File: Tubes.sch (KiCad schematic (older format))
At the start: 36 parts

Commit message: Finished draft schema
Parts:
- gave numbers to parts that had none: 36

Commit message: Finished schema and started PCB layout
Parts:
- R1, R10, R11, R12, R13, R14, R15, R16, R17, R18, R2, R3, R4, R5, R6, R7, R8, R9: footprint (none) -> Resistor_THT:R_Axial_DIN0207_L6.3mm_D2.5mm_P10.16mm_Horizontal
- U10, U2, U3, U4, U8, U9: footprint (none) -> nixies:Nixie_ZM1000
- U11, U12, U13, U5, U6, U7: footprint (none) -> Package_DIP:DIP-16_W7.62mm_LongPads
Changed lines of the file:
@@
 F 0 "U10" H 9828 5003 60  0000 L CNN
 F 1 "ZM1000" H 9828 4897 60  0000 L CNN
-F 2 "" V 8950 4600 60  0001 C CNN
+F 2 "nixies:Nixie_ZM1000" V 8950 4600 60  0001 C CNN
 F 3 "" V 8950 4600 60  0001 C CNN
 	1    8800 4650
@@
 F 0 "U9" H 6228 5003 60  0000 L CNN
 F 1 "ZM1000" H 6228 4897 60  0000 L CNN
-F 2 "" V 5350 4600 60  0001 C CNN
+F 2 "nixies:Nixie_ZM1000" V 5350 4600 60  0001 C CNN
 F 3 "" V 5350 4600 60  0001 C CNN
 	1    5200 4650
@@
 F 0 "U8" H 2628 5003 60  0000 L CNN
 F 1 "ZM1000" H 2628 4897 60  0000 L CNN
-F 2 "" V 1750 4600 60  0001 C CNN
+F 2 "nixies:Nixie_ZM1000" V 1750 4600 60  0001 C CNN
 F 3 "" V 1750 4600 60  0001 C CNN
 	1    1600 4650
@@
 F 0 "U2" H 2628 2303 60  0000 L CNN
 F 1 "ZM1000" H 2628 2197 60  0000 L CNN
-F 2 "" V 1750 1900 60  0001 C CNN
+F 2 "nixies:Nixie_ZM1000" V 1750 1900 60  0001 C CNN
 F 3 "" V 1750 1900 60  0001 C CNN
 	1    1600 1950
@@
 F 0 "U3" H 6228 2303 60  0000 L CNN
 F 1 "ZM1000" H 6228 2197 60  0000 L CNN
-F 2 "" V 5350 1900 60  0001 C CNN
+F 2 "nixies:Nixie_ZM1000" V 5350 1900 60  0001 C CNN
 F 3 "" V 5350 1900 60  0001 C CNN
 	1    5200 1950
@@
 F 0 "U4" H 9828 2303 60  0000 L CNN
 F 1 "ZM1000" H 9828 2197 60  0000 L CNN
-F 2 "" V 8950 1900 60  0001 C CNN
+F 2 "nixies:Nixie_ZM1000" V 8950 1900 60  0001 C CNN
 F 3 "" V 8950 1900 60  0001 C CNN
 	1    8800 1950
@@
 F 0 "U13" V 9800 5200 50  0000 R CNN
 F 1 "SN74141" V 9800 4850 50  0000 R CNN
-F 2 "" H 9900 4900 50  0001 C CNN
+F 2 "Package_DIP:DIP-16_W7.62mm_LongPads" H 9900 4900 50  0001 C CNN
 F 3 "http://www.ti.com/lit/ds/symlink/sn74hc595.pdf" H 9900 4900 50  0001 C CNN
 	1    9900 4850
@@
 F 0 "R16" V 9407 3900 50  0000 C CNN
 F 1 "10M" V 9316 3900 50  0000 C CNN
-F 2 "" V 9130 3900 50  0001 C CNN
+F 2 "Resistor_THT:R_Axial_DIN0207_L6.3mm_D2.5mm_P10.16mm_Horizontal" V 9130 3900 50  0001 C CNN
 F 3 "~" H 9200 3900 50  0001 C CNN
 	1    9200 3900
@@
 F 0 "U12" V 6200 5200 50  0000 R CNN
 F 1 "SN74141" V 6200 4850 50  0000 R CNN
-F 2 "" H 6300 4900 50  0001 C CNN
+F 2 "Package_DIP:DIP-16_W7.62mm_LongPads" H 6300 4900 50  0001 C CNN
 F 3 "http://www.ti.com/lit/ds/symlink/sn74hc595.pdf" H 6300 4900 50  0001 C CNN
 	1    6300 4850
@@
 $EndComp
 Wire Wire Line
-	6300 4200 6300 4100
-Wire Wire Line
 	6300 4100 6400 4100
 Text HLabel 6800 5000 2    50   Input ~ 0
@@
 F 0 "R13" V 5807 3900 50  0000 C CNN
 F 1 "10M" V 5716 3900 50  0000 C CNN
-F 2 "" V 5530 3900 50  0001 C CNN
+F 2 "Resistor_THT:R_Axial_DIN0207_L6.3mm_D2.5mm_P10.16mm_Horizontal" V 5530 3900 50  0001 C CNN
 F 3 "~" H 5600 3900 50  0001 C CNN
 	1    5600 3900
@@
 F 0 "U11" V 2600 5200 50  0000 R CNN
 F 1 "SN74141" V 2600 4850 50  0000 R CNN
-F 2 "" H 2700 4900 50  0001 C CNN
+F 2 "Package_DIP:DIP-16_W7.62mm_LongPads" H 2700 4900 50  0001 C CNN
 F 3 "http://www.ti.com/lit/ds/symlink/sn74hc595.pdf" H 2700 4900 50  0001 C CNN
 	1    2700 4850
@@
 F 0 "R10" V 2207 3900 50  0000 C CNN
 F 1 "10M" V 2116 3900 50  0000 C CNN
-F 2 "" V 1930 3900 50  0001 C CNN
+F 2 "Resistor_THT:R_Axial_DIN0207_L6.3mm_D2.5mm_P10.16mm_Horizontal" V 1930 3900 50  0001 C CNN
 F 3 "~" H 2000 3900 50  0001 C CNN
 	1    2000 3900
@@
 F 0 "U5" V 2600 2500 50  0000 R CNN
 F 1 "SN74141" V 2600 2150 50  0000 R CNN
-F 2 "" H 2700 2200 50  0001 C CNN
+F 2 "Package_DIP:DIP-16_W7.62mm_LongPads" H 2700 2200 50  0001 C CNN
 F 3 "http://www.ti.com/lit/ds/symlink/sn74hc595.pdf" H 2700 2200 50  0001 C CNN
 	1    2700 2150
@@
 F 0 "R1" V 2207 1200 50  0000 C CNN
 F 1 "10M" V 2116 1200 50  0000 C CNN
-F 2 "" V 1930 1200 50  0001 C CNN
+F 2 "Resistor_THT:R_Axial_DIN0207_L6.3mm_D2.5mm_P10.16mm_Horizontal" V 1930 1200 50  0001 C CNN
 F 3 "~" H 2000 1200 50  0001 C CNN
 	1    2000 1200
@@
 F 0 "U6" V 6200 2500 50  0000 R CNN
 F 1 "SN74141" V 6200 2150 50  0000 R CNN
-F 2 "" H 6300 2200 50  0001 C CNN
+F 2 "Package_DIP:DIP-16_W7.62mm_LongPads" H 6300 2200 50  0001 C CNN
 F 3 "http://www.ti.com/lit/ds/symlink/sn74hc595.pdf" H 6300 2200 50  0001 C CNN
 	1    6300 2150
@@
 	0    -1   -1   0
 $EndComp
-Wire Wire Line
-	6300 1500 6300 1400
-Wire Wire Line
-	6300 1400 6400 1400
 Text HLabel 6800 2300 2    50   Input ~ 0
 BCD_T2A
@@
 F 0 "R4" V 5807 1200 50  0000 C CNN
 F 1 "10M" V 5716 1200 50  0000 C CNN
-F 2 "" V 5530 1200 50  0001 C CNN
+F 2 "Resistor_THT:R_Axial_DIN0207_L6.3mm_D2.5mm_P10.16mm_Horizontal" V 5530 1200 50  0001 C CNN
 F 3 "~" H 5600 1200 50  0001 C CNN
 	1    5600 1200
@@
 F 0 "U7" V 9800 2500 50  0000 R CNN
 F 1 "SN74141" V 9800 2150 50  0000 R CNN
-F 2 "" H 9900 2200 50  0001 C CNN
+F 2 "Package_DIP:DIP-16_W7.62mm_LongPads" H 9900 2200 50  0001 C CNN
 F 3 "http://www.ti.com/lit/ds/symlink/sn74hc595.pdf" H 9900 2200 50  0001 C CNN
 	1    9900 2150
@@
 F 0 "R7" V 9407 1200 50  0000 C CNN
 F 1 "10M" V 9316 1200 50  0000 C CNN
-F 2 "" V 9130 1200 50  0001 C CNN
+F 2 "Resistor_THT:R_Axial_DIN0207_L6.3mm_D2.5mm_P10.16mm_Horizontal" V 9130 1200 50  0001 C CNN
 F 3 "~" H 9200 1200 50  0001 C CNN
 	1    9200 1200
@@
 F 0 "R3" V 3457 1200 50  0000 C CNN
 F 1 "10k" V 3366 1200 50  0000 C CNN
-F 2 "" V 3180 1200 50  0001 C CNN
+F 2 "Resistor_THT:R_Axial_DIN0207_L6.3mm_D2.5mm_P10.16mm_Horizontal" V 3180 1200 50  0001 C CNN
 F 3 "~" H 3250 1200 50  0001 C CNN
 	1    3250 1200
@@
 F 0 "R2" H 2270 1246 50  0000 L CNN
 F 1 "100k" H 2270 1155 50  0000 L CNN
-F 2 "" V 2130 1200 50  0001 C CNN
+F 2 "Resistor_THT:R_Axial_DIN0207_L6.3mm_D2.5mm_P10.16mm_Horizontal" V 2130 1200 50  0001 C CNN
 F 3 "~" H 2200 1200 50  0001 C CNN
 	1    2200 1200
@@
 F 0 "R6" V 7057 1200 50  0000 C CNN
 F 1 "10k" V 6966 1200 50  0000 C CNN
-F 2 "" V 6780 1200 50  0001 C CNN
+F 2 "Resistor_THT:R_Axial_DIN0207_L6.3mm_D2.5mm_P10.16mm_Horizontal" V 6780 1200 50  0001 C CNN
 F 3 "~" H 6850 1200 50  0001 C CNN
 	1    6850 1200
@@
 F 0 "R5" H 5870 1246 50  0000 L CNN
 F 1 "100k" H 5870 1155 50  0000 L CNN
-F 2 "" V 5730 1200 50  0001 C CNN
+F 2 "Resistor_THT:R_Axial_DIN0207_L6.3mm_D2.5mm_P10.16mm_Horizontal" V 5730 1200 50  0001 C CNN
 F 3 "~" H 5800 1200 50  0001 C CNN
 	1    5800 1200
@@
 F 0 "R9" V 10657 1200 50  0000 C CNN
 F 1 "10k" V 10566 1200 50  0000 C CNN
-F 2 "" V 10380 1200 50  0001 C CNN
+F 2 "Resistor_THT:R_Axial_DIN0207_L6.3mm_D2.5mm_P10.16mm_Horizontal" V 10380 1200 50  0001 C CNN
 F 3 "~" H 10450 1200 50  0001 C CNN
 	1    10450 1200
@@
 F 0 "R8" H 9470 1246 50  0000 L CNN
 F 1 "100k" H 9470 1155 50  0000 L CNN
-F 2 "" V 9330 1200 50  0001 C CNN
+F 2 "Resistor_THT:R_Axial_DIN0207_L6.3mm_D2.5mm_P10.16mm_Horizontal" V 9330 1200 50  0001 C CNN
 F 3 "~" H 9400 1200 50  0001 C CNN
 	1    9400 1200
@@
 F 0 "R18" V 10657 3900 50  0000 C CNN
 F 1 "10k" V 10566 3900 50  0000 C CNN
-F 2 "" V 10380 3900 50  0001 C CNN
+F 2 "Resistor_THT:R_Axial_DIN0207_L6.3mm_D2.5mm_P10.16mm_Horizontal" V 10380 3900 50  0001 C CNN
 F 3 "~" H 10450 3900 50  0001 C CNN
 	1    10450 3900
@@
 F 0 "R17" H 9470 3946 50  0000 L CNN
 F 1 "100k" H 9470 3855 50  0000 L CNN
-F 2 "" V 9330 3900 50  0001 C CNN
+F 2 "Resistor_THT:R_Axial_DIN0207_L6.3mm_D2.5mm_P10.16mm_Horizontal" V 9330 3900 50  0001 C CNN
 F 3 "~" H 9400 3900 50  0001 C CNN
 	1    9400 3900
@@
 F 0 "R15" V 7057 3900 50  0000 C CNN
 F 1 "10k" V 6966 3900 50  0000 C CNN
-F 2 "" V 6780 3900 50  0001 C CNN
+F 2 "Resistor_THT:R_Axial_DIN0207_L6.3mm_D2.5mm_P10.16mm_Horizontal" V 6780 3900 50  0001 C CNN
 F 3 "~" H 6850 3900 50  0001 C CNN
 	1    6850 3900
@@
 F 0 "R14" H 5870 3946 50  0000 L CNN
 F 1 "100k" H 5870 3855 50  0000 L CNN
-F 2 "" V 5730 3900 50  0001 C CNN
+F 2 "Resistor_THT:R_Axial_DIN0207_L6.3mm_D2.5mm_P10.16mm_Horizontal" V 5730 3900 50  0001 C CNN
 F 3 "~" H 5800 3900 50  0001 C CNN
 	1    5800 3900
@@
 F 0 "R12" V 3457 3900 50  0000 C CNN
 F 1 "10k" V 3366 3900 50  0000 C CNN
-F 2 "" V 3180 3900 50  0001 C CNN
+F 2 "Resistor_THT:R_Axial_DIN0207_L6.3mm_D2.5mm_P10.16mm_Horizontal" V 3180 3900 50  0001 C CNN
 F 3 "~" H 3250 3900 50  0001 C CNN
 	1    3250 3900
@@
 F 0 "R11" H 2270 3946 50  0000 L CNN
 F 1 "100k" H 2270 3855 50  0000 L CNN
-F 2 "" V 2130 3900 50  0001 C CNN
+F 2 "Resistor_THT:R_Axial_DIN0207_L6.3mm_D2.5mm_P10.16mm_Horizontal" V 2130 3900 50  0001 C CNN
 F 3 "~" H 2200 3900 50  0001 C CNN
 	1    2200 3900
@@
 Wire Wire Line
 	2200 3500 2800 3500
+Wire Wire Line
+	6300 4100 6300 4200
+Wire Wire Line
+	6400 1400 6300 1400
+Wire Wire Line
+	6300 1400 6300 1500
 $EndSCHEMATC

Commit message: Szitched to DIP shift registers, added BME280
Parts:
- U11, U12, U13, U5, U6, U7: footprint Package_DIP:DIP-16_W7.62mm_LongPads -> Package_DIP:DIP-16_W7.62mm
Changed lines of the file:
@@
 F 0 "U13" V 9800 5200 50  0000 R CNN
 F 1 "SN74141" V 9800 4850 50  0000 R CNN
-F 2 "Package_DIP:DIP-16_W7.62mm_LongPads" H 9900 4900 50  0001 C CNN
+F 2 "Package_DIP:DIP-16_W7.62mm" H 9900 4900 50  0001 C CNN
 F 3 "http://www.ti.com/lit/ds/symlink/sn74hc595.pdf" H 9900 4900 50  0001 C CNN
 	1    9900 4850
@@
 F 0 "U12" V 6200 5200 50  0000 R CNN
 F 1 "SN74141" V 6200 4850 50  0000 R CNN
-F 2 "Package_DIP:DIP-16_W7.62mm_LongPads" H 6300 4900 50  0001 C CNN
+F 2 "Package_DIP:DIP-16_W7.62mm" H 6300 4900 50  0001 C CNN
 F 3 "http://www.ti.com/lit/ds/symlink/sn74hc595.pdf" H 6300 4900 50  0001 C CNN
 	1    6300 4850
@@
 F 0 "U11" V 2600 5200 50  0000 R CNN
 F 1 "SN74141" V 2600 4850 50  0000 R CNN
-F 2 "Package_DIP:DIP-16_W7.62mm_LongPads" H 2700 4900 50  0001 C CNN
+F 2 "Package_DIP:DIP-16_W7.62mm" H 2700 4900 50  0001 C CNN
 F 3 "http://www.ti.com/lit/ds/symlink/sn74hc595.pdf" H 2700 4900 50  0001 C CNN
 	1    2700 4850
@@
 F 0 "U5" V 2600 2500 50  0000 R CNN
 F 1 "SN74141" V 2600 2150 50  0000 R CNN
-F 2 "Package_DIP:DIP-16_W7.62mm_LongPads" H 2700 2200 50  0001 C CNN
+F 2 "Package_DIP:DIP-16_W7.62mm" H 2700 2200 50  0001 C CNN
 F 3 "http://www.ti.com/lit/ds/symlink/sn74hc595.pdf" H 2700 2200 50  0001 C CNN
 	1    2700 2150
@@
 F 0 "U6" V 6200 2500 50  0000 R CNN
 F 1 "SN74141" V 6200 2150 50  0000 R CNN
-F 2 "Package_DIP:DIP-16_W7.62mm_LongPads" H 6300 2200 50  0001 C CNN
+F 2 "Package_DIP:DIP-16_W7.62mm" H 6300 2200 50  0001 C CNN
 F 3 "http://www.ti.com/lit/ds/symlink/sn74hc595.pdf" H 6300 2200 50  0001 C CNN
 	1    6300 2150
@@
 F 0 "U7" V 9800 2500 50  0000 R CNN
 F 1 "SN74141" V 9800 2150 50  0000 R CNN
-F 2 "Package_DIP:DIP-16_W7.62mm_LongPads" H 9900 2200 50  0001 C CNN
+F 2 "Package_DIP:DIP-16_W7.62mm" H 9900 2200 50  0001 C CNN
 F 3 "http://www.ti.com/lit/ds/symlink/sn74hc595.pdf" H 9900 2200 50  0001 C CNN
 	1    9900 2150

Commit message: Final pending check
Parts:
- U10, U2, U3, U4, U8, U9: symbol Nixies:ZM1000 -> nixieClock_ZM1000-rescue:ZM1000-Nixies
- U11, U12, U13, U5, U6, U7: symbol Nixies:SN74141 -> nixieClock_ZM1000-rescue:SN74141-Nixies
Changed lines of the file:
@@
 $EndDescr
 $Comp
-L Nixies:ZM1000 U10
+L nixieClock_ZM1000-rescue:ZM1000-Nixies U10
 U 1 1 5D979FEC
 P 8800 4650
@@
 $EndComp
 $Comp
-L Nixies:ZM1000 U9
+L nixieClock_ZM1000-rescue:ZM1000-Nixies U9
 U 1 1 5D980CEC
 P 5200 4650
@@
 $EndComp
 $Comp
-L Nixies:ZM1000 U8
+L nixieClock_ZM1000-rescue:ZM1000-Nixies U8
 U 1 1 5D98680C
 P 1600 4650
@@
 $EndComp
 $Comp
-L Nixies:ZM1000 U2
+L nixieClock_ZM1000-rescue:ZM1000-Nixies U2
 U 1 1 5D988EF7
 P 1600 1950
@@
 $EndComp
 $Comp
-L Nixies:ZM1000 U3
+L nixieClock_ZM1000-rescue:ZM1000-Nixies U3
 U 1 1 5D988F01
 P 5200 1950
@@
 $EndComp
 $Comp
-L Nixies:ZM1000 U4
+L nixieClock_ZM1000-rescue:ZM1000-Nixies U4
 U 1 1 5D988F0B
 P 8800 1950
@@
 $EndComp
 $Comp
-L Nixies:SN74141 U13
+L nixieClock_ZM1000-rescue:SN74141-Nixies U13
 U 1 1 5D8DD700
 P 9900 4850
 AR Path="/5D904EA9/5D8DD700" Ref="U13"  Part="1"
 AR Path="/5DB44C0F/5D8DD700" Ref="U?"  Part="1"
+AR Path="/5D8DD700" Ref="U13"  Part="1"
 F 0 "U13" V 9800 5200 50  0000 R CNN
 F 1 "SN74141" V 9800 4850 50  0000 R CNN
@@
 	9200 4200 9200 4050
 $Comp
-L Nixies:SN74141 U12
+L nixieClock_ZM1000-rescue:SN74141-Nixies U12
 U 1 1 5D92735A
 P 6300 4850
 AR Path="/5D904EA9/5D92735A" Ref="U12"  Part="1"
 AR Path="/5DB44C0F/5D92735A" Ref="U?"  Part="1"
+AR Path="/5D92735A" Ref="U12"  Part="1"
 F 0 "U12" V 6200 5200 50  0000 R CNN
 F 1 "SN74141" V 6200 4850 50  0000 R CNN
@@
 HV
 $Comp
-L Nixies:SN74141 U11
+L nixieClock_ZM1000-rescue:SN74141-Nixies U11
 U 1 1 5D92C1CA
 P 2700 4850
 AR Path="/5D904EA9/5D92C1CA" Ref="U11"  Part="1"
 AR Path="/5DB44C0F/5D92C1CA" Ref="U?"  Part="1"
+AR Path="/5D92C1CA" Ref="U11"  Part="1"
 F 0 "U11" V 2600 5200 50  0000 R CNN
 F 1 "SN74141" V 2600 4850 50  0000 R CNN
@@
 BCD_T6D
 $Comp
-L Nixies:SN74141 U5
+L nixieClock_ZM1000-rescue:SN74141-Nixies U5
 U 1 1 5D94B1B0
 P 2700 2150
 AR Path="/5D904EA9/5D94B1B0" Ref="U5"  Part="1"
 AR Path="/5DB44C0F/5D94B1B0" Ref="U?"  Part="1"
+AR Path="/5D94B1B0" Ref="U5"  Part="1"
 F 0 "U5" V 2600 2500 50  0000 R CNN
 F 1 "SN74141" V 2600 2150 50  0000 R CNN
@@
 	2000 1500 2000 1350
 $Comp
-L Nixies:SN74141 U6
+L nixieClock_ZM1000-rescue:SN74141-Nixies U6
 U 1 1 5D94B1F1
 P 6300 2150
 AR Path="/5D904EA9/5D94B1F1" Ref="U6"  Part="1"
 AR Path="/5DB44C0F/5D94B1F1" Ref="U?"  Part="1"
+AR Path="/5D94B1F1" Ref="U6"  Part="1"
 F 0 "U6" V 6200 2500 50  0000 R CNN
 F 1 "SN74141" V 6200 2150 50  0000 R CNN
@@
 	5600 1500 5600 1350
 $Comp
-L Nixies:SN74141 U7
+L nixieClock_ZM1000-rescue:SN74141-Nixies U7
 U 1 1 5D94B233
 P 9900 2150
 AR Path="/5D904EA9/5D94B233" Ref="U7"  Part="1"
 AR Path="/5DB44C0F/5D94B233" Ref="U?"  Part="1"
+AR Path="/5D94B233" Ref="U7"  Part="1"
 F 0 "U7" V 9800 2500 50  0000 R CNN
 F 1 "SN74141" V 9800 2150 50  0000 R CNN

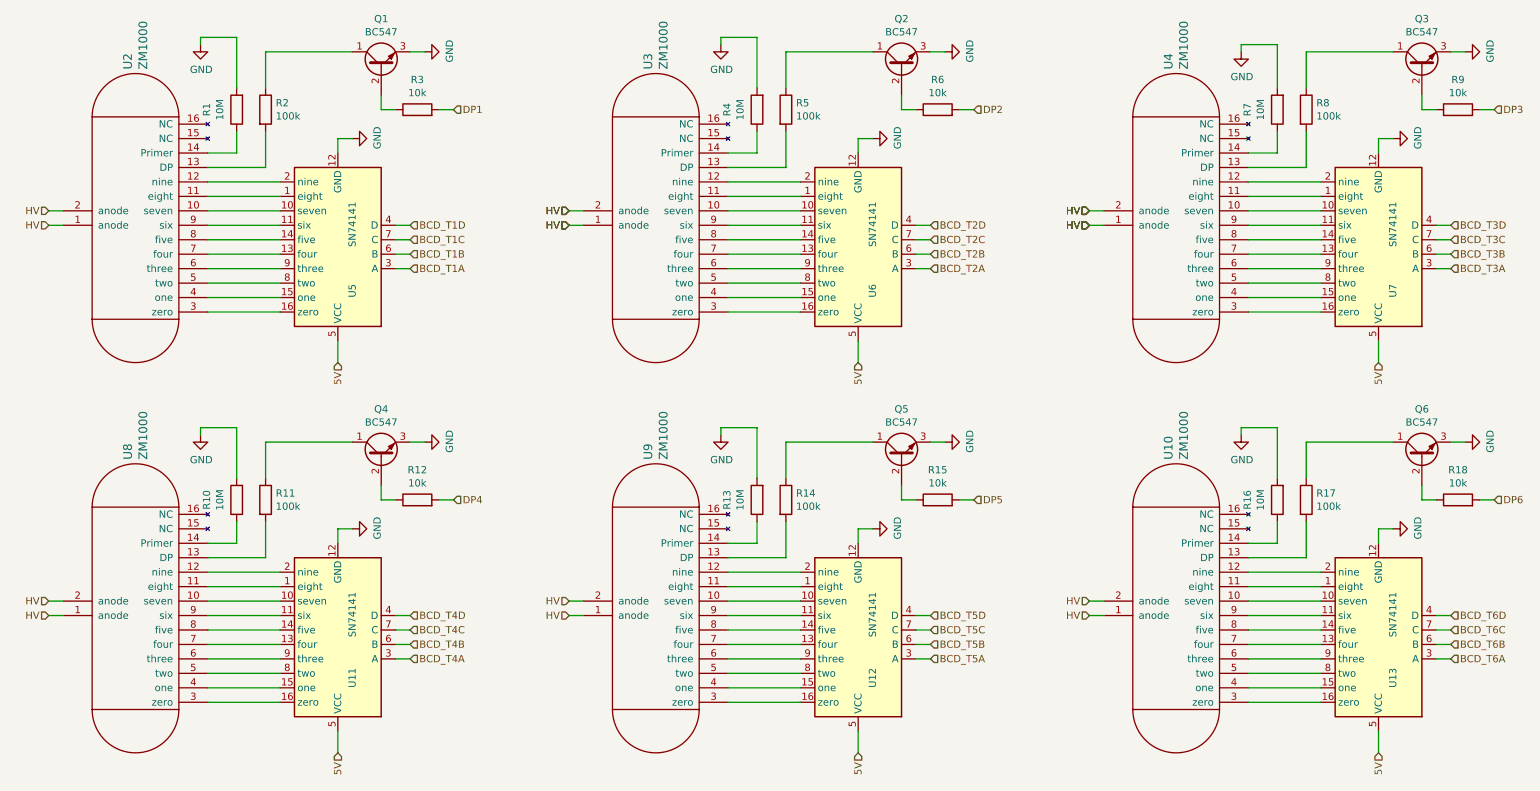
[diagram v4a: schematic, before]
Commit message: Fixed tube footprints and rerouted
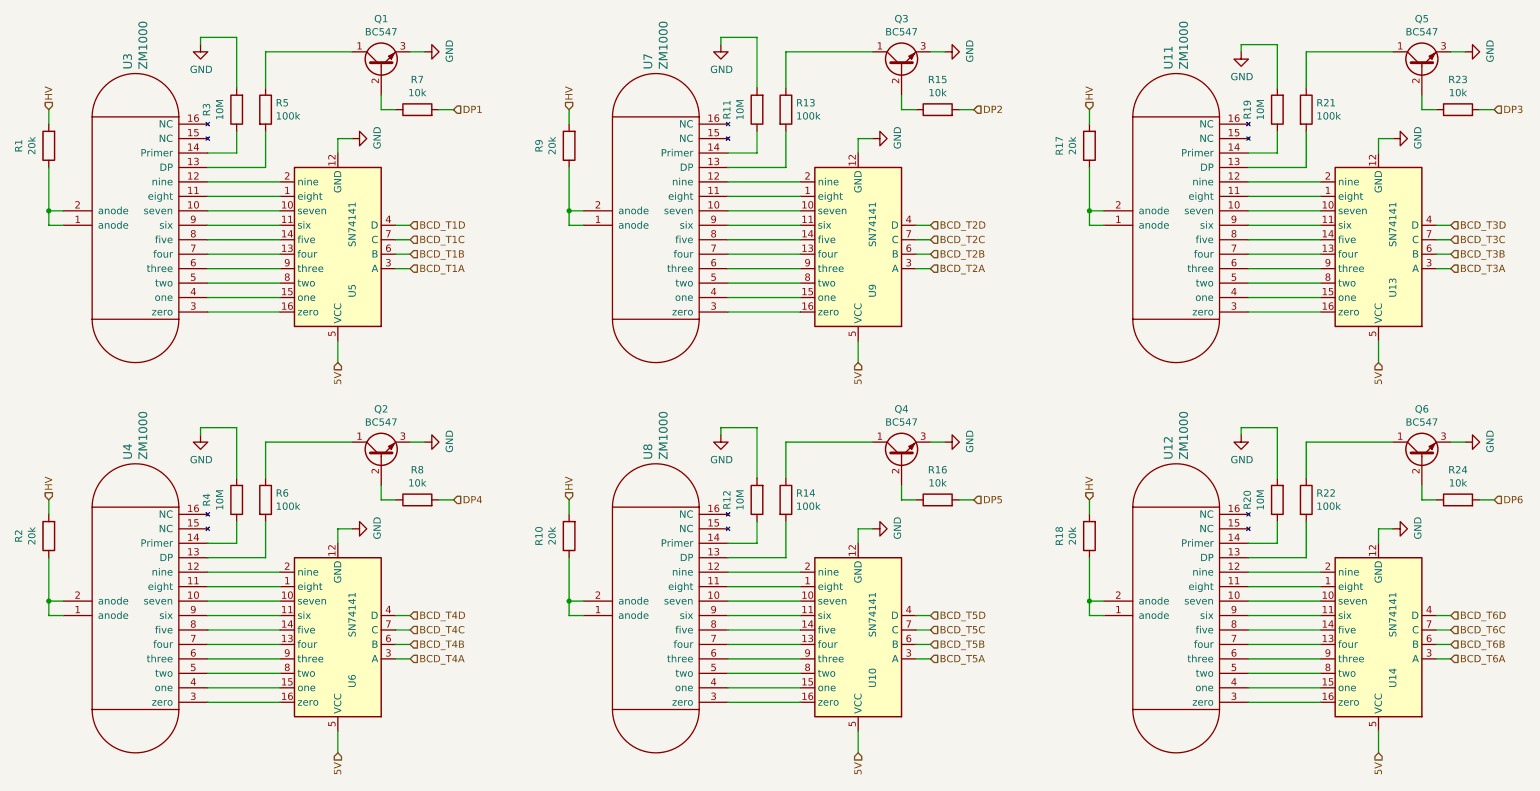
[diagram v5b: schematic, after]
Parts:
- added R1, R10, R17, R18, R2, R9: 20k, Resistor_THT:R_Axial_DIN0207_L6.3mm_D2.5mm_P10.16mm_Horizontal, symbol Device:R
- renumbered Q4 to Q2, Q2 to Q3, Q5 to Q4, Q3 to Q5, R4 to R11, R13 to R12, R5 to R13, R6 to R15, R15 to R16, R7 to R19, R16 to R20, R8 to R21, R17 to R22, R9 to R23, R18 to R24, R1 to R3, R10 to R4, R2 to R5, R11 to R6, R3 to R7, R12 to R8, U12 to U10, U4 to U11, U10 to U12, U7 to U13, U13 to U14, U2 to U3, U8 to U4, U11 to U6, U3 to U7, U9 to U8, U6 to U9
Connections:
- net HV: now also R1.2, R10.2, R17.2, R18.2, R2.2, R9.2; no longer U11.1 (anode), U11.2 (anode), U12.1 (anode), U12.2 (anode), U3.1 (anode), U3.2 (anode), U4.1 (anode), U4.2 (anode), U7.1 (anode), U7.2 (anode), U8.1 (anode), U8.2 (anode)
- new net: R18.1, U12.1 (anode), U12.2 (anode)
- new net: R10.1, U8.1 (anode), U8.2 (anode)
- new net: R2.1, U4.1 (anode), U4.2 (anode)
- new net: R1.1, U3.1 (anode), U3.2 (anode)
- new net: R9.1, U7.1 (anode), U7.2 (anode)
- new net: R17.1, U11.1 (anode), U11.2 (anode)
